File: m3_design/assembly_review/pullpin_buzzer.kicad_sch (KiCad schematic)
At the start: 10 parts, among them J123 BM02B-GHS-TBT(LF)(SN), Q123 AO3400A

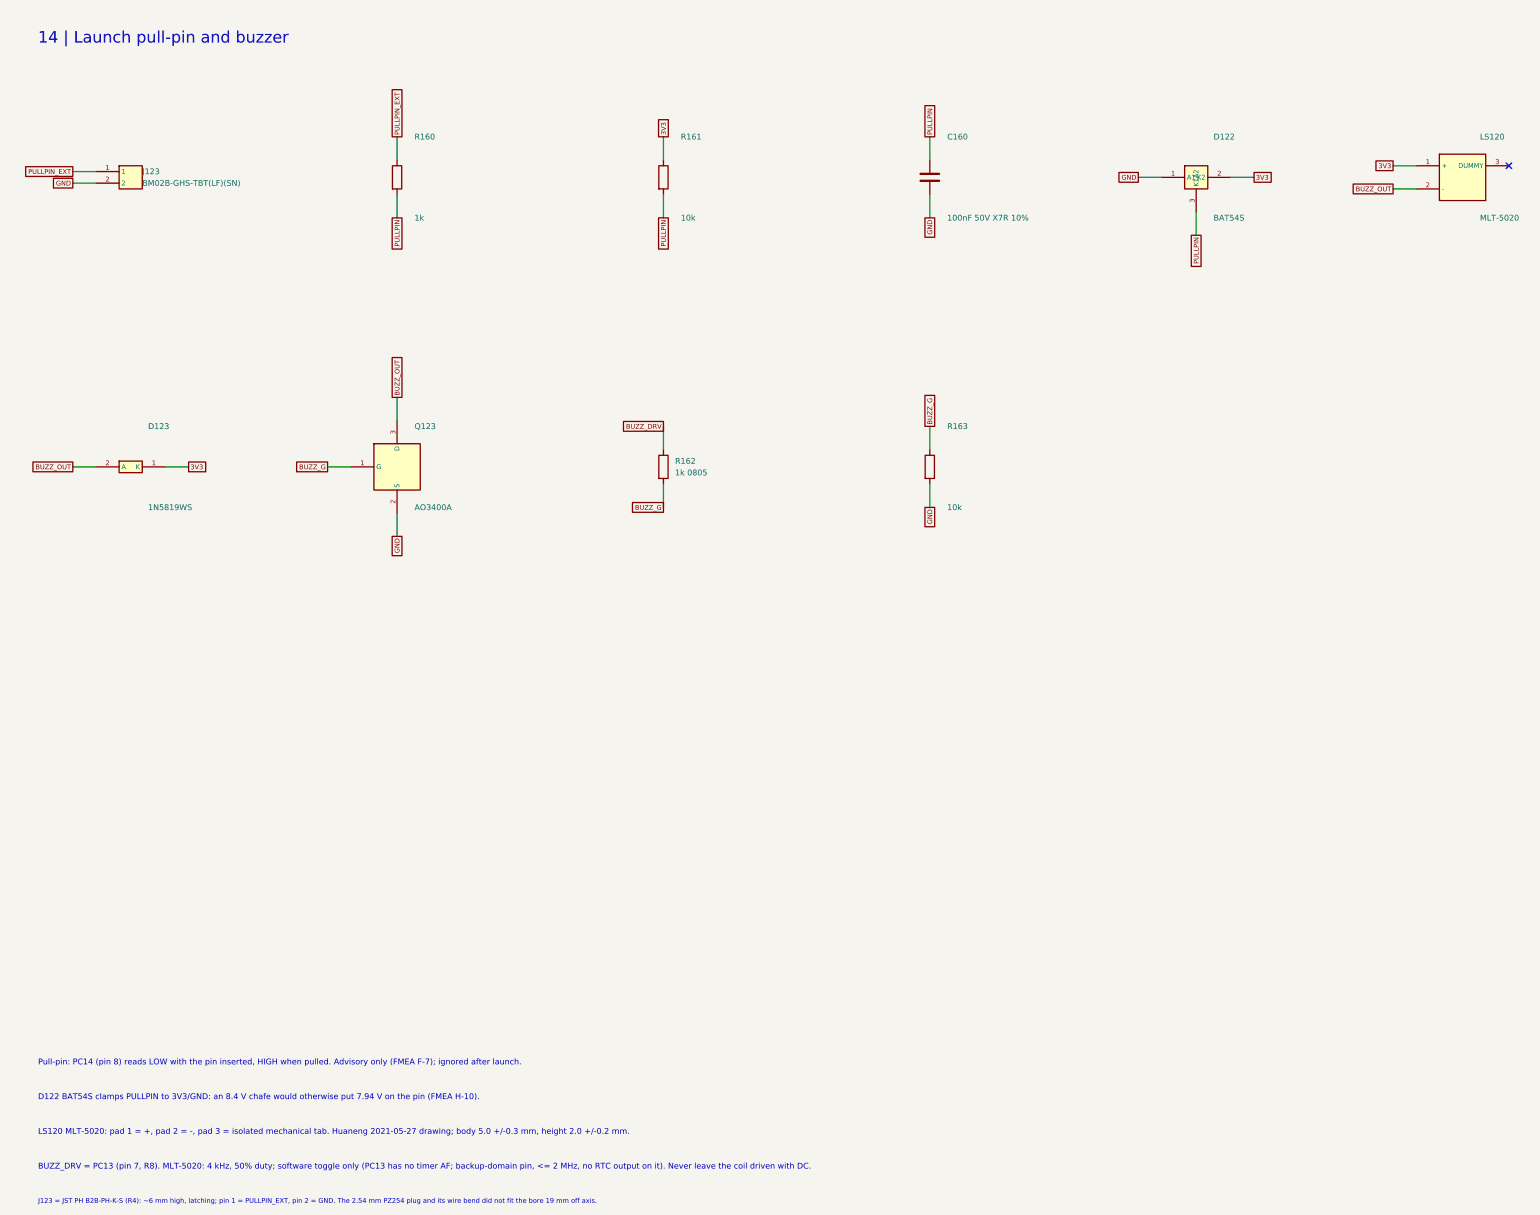
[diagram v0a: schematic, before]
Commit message: R10 requirements-audit cuts and GAP fixes before review round 9
Implement adopted AUD-1 through AUD-10 and GAP-1 through GAP-5 after the single-switch pass.
Remove the advisory pull-pin, redundant probes and GPS/radio IO LDO cells; qualify the smaller
AONR21357 pair, correct C120 voltage rating, standardize shared-code capacitor lands, simplify
slow returns and fire-only copper, localize U9 output protection and add exactly two U401 VIPPO vias.
Record physical-current timing, coupled fire/source budget, C84 manual fitting and narrowed gate scopes.

Board SHA-256: 877d01996a59e9dd5c6dbc367274bb9a323a13982d67960fe46df9b0ee53205d
Board: 46 x 90 mm, 4 layers, 2365477 bytes; 225 footprints, 883 straight tracks, 323 vias.
Netlist SHA-256: 0843da709e2d7a757e9b35cdff48158a54012c5353619cbf409ab961efd2c3ca
Two fresh complete passing builds are byte-identical. Schematic: 700 pins; 22 seeded faults detected.

Final unskipped tools/check.sh: exit 0
DRC violations 0  unconnected 0  schematic parity 0  ERC 0
metadata / 3D model audit: OK
silkscreen outside the board outline: 0 stroke points
fit check: OK (CAD envelopes only)
R10 CAD contract (full): OK
routing hygiene: 0 failing, 0 allowlisted, 0 leftovers recorded
actuator safety contract: OK
Fab manifest: OK; 5 outputs match current CAD and export inputs
Self-tests: shell 4, fit 24, paste 5, routing 59, R10 131; three NumPy cases rerun and passed.

Fab: 215 CPL rows, 82 BOM codes; orientation / paste / manifest pass. Hot-plug: 2304 required
cases plus convergence and controls pass (simulation / Inference). Plate f1 280.9 Hz (Inference).
Live JLC: $84.43 vs $84.41 target, 46 Extended codes; R430 / U4 short. Procurement exit 1 is a
disclosed OQ-3 / ordering deviation, not a CAD gate pass. No quote accepted or order placed.
Firmware, bench, thermal/transient correlation, process acceptance, installed RF immunity and physical fit unverified.

This preparatory pass earns no clean-review credit. Start fresh full ten-lens round 9 on th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
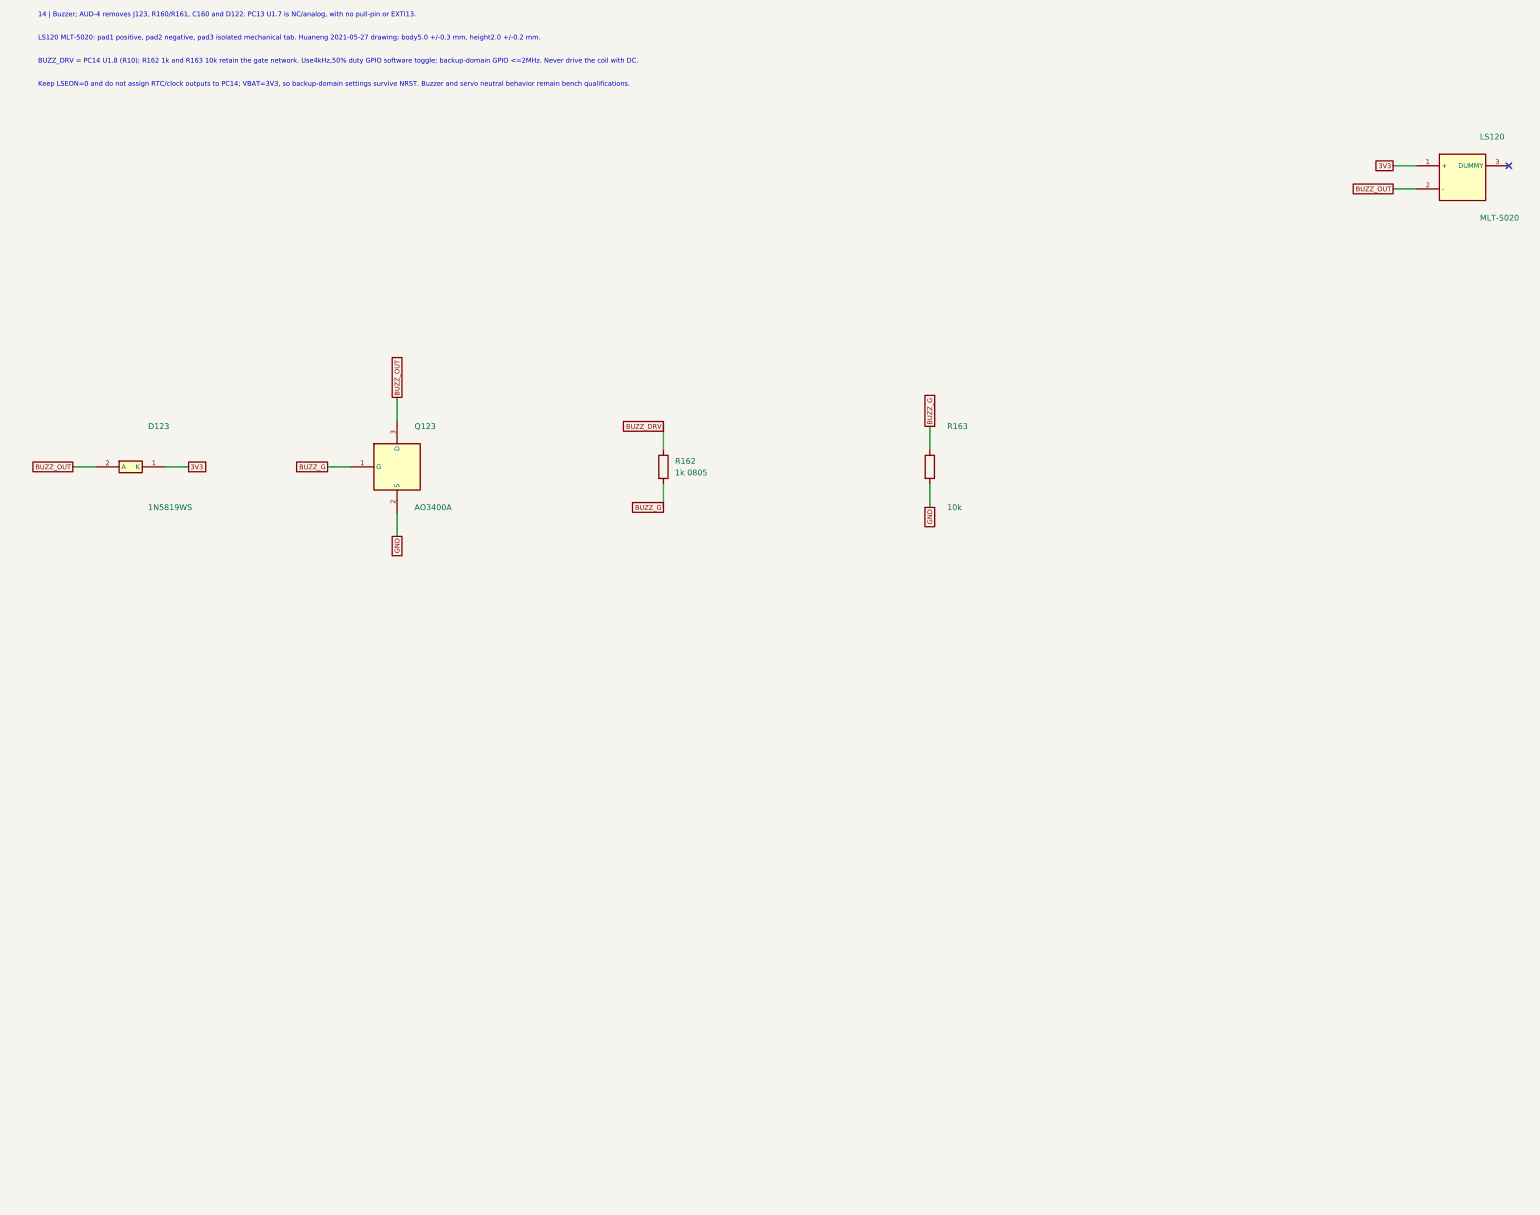
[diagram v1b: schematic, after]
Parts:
- removed C160: 100nF 50V X7R 10%, rocket:C0402, symbol M3:C
- removed D122: BAT54S, rocket:SOT-23-3_L2.9-W1.3-P1.90-LS2.4-BR, symbol M3:BAT54S
- removed J123: BM02B-GHS-TBT(LF)(SN), rocket:M3_GH_BM02B_GHS_TBT, symbol M3:Conn_1x2
- removed R160: 1k, rocket:R0402, symbol M3:R
- removed R161: 10k, rocket:R0402, symbol M3:R
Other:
- note added: "14 | Buzzer; AUD-4 removes J123, R160/R161, C160 and D122. PC13 U1.7 is NC/analog, with no pull-pin or EXTI13."
- note added: "BUZZ_DRV = PC14 U1.8 (R10); R162 1k and R163 10k retain the gate network. Use4kHz,50% duty GPIO software toggle; backup-domain GPIO <=2MHz. Never drive the coil with DC."
- note added: "Keep LSEON=0 and do not assign RTC/clock outputs to PC14; VBAT=3V3, so backup-domain settings survive NRST. Buzzer and servo neutral behavior remain bench qualifications."
- note added: "LS120 MLT-5020: pad1 positive, pad2 negative, pad3 isolated mechanical tab. Huaneng 2021-05-27 drawing; body5.0 +/-0.3 mm, height2.0 +/-0.2 mm."
- note removed: "14 | Launch pull-pin and buzzer"
- note removed: "BUZZ_DRV = PC13 (pin 7, R8). MLT-5020: 4 kHz, 50% duty; software toggle only (PC13 has no timer AF; backup-domain pin, <= 2 MHz, no RTC output on it). Never leave the coil driven with DC."
- note removed: "D122 BAT54S clamps PULLPIN to 3V3/GND: an 8.4 V chafe would otherwise put 7.94 V on the pin (FMEA H-10)."
- note removed: "J123 = JST PH B2B-PH-K-S (R4): ~6 mm high, latching; pin 1 = PULLPIN_EXT, pin 2 = GND. The 2.54 mm PZ254 plug and its wire bend did not fit the bore 19 mm off axis."
- note removed: "LS120 MLT-5020: pad 1 = +, pad 2 = -, pad 3 = isolated mechanical tab. Huaneng 2021-05-27 drawing; body 5.0 +/-0.3 mm, height 2.0 +/-0.2 mm."
- note removed: "Pull-pin: PC14 (pin 8) reads LOW with the pin inserted, HIGH when pulled. Advisory only (FMEA F-7); ignored after launch."
- title: 14 | Launch pull-pin and buzzer -> 14 | Buzzer
